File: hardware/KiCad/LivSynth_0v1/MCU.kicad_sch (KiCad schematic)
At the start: 19 parts, among them J2 SWD, J3 USB_B_Micro, SW1 SW_SPDT, U9 STM32F405RGT6, Y1 ABM8-16

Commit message: Fill all title blocks
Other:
- title: (none) -> LivSynth - MCU
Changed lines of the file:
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@@
   (paper "A4")
   (title_block
+    (title "LivSynth - MCU")
     (date "2022-07-18")
     (rev "${Version}")

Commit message: Initial Routing finished
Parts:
- added NT1: NetTie_2, NetTie:NetTie-2_SMD_Pad2.0mm, symbol Device:NetTie_2
- C20: footprint Capacitor_SMD:C_0603_1608Metric_Pad1.08x0.95mm_HandSolder -> Capacitor_THT:CP_Radial_D8.0mm_P5.00mm
- J3: footprint (none) -> Connector_USB:USB_Micro-B_Wuerth_629105150521
- SW1: footprint Capacitor_THT:C_Disc_D3.0mm_W1.6mm_P2.50mm -> Button_Switch_THT:SW_E-Switch_EG1224_SPDT_Angled
- Y1: footprint (none) -> Crystal:Crystal_SMD_3225-4Pin_3.2x2.5mm_HandSoldering
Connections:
- net DAC_OUT2 is gone; now on net SPI_SCK: U9.21 (PA5)
- net CLOCK_OUT: now also U9.24 (PC4); no longer U9.22 (PA6)
- net GATE_OUT: now also U9.26 (PB0); no longer U9.24 (PC4)
- net GND: now also NT1.1; no longer J3.5 (GND)
- net RESET_OUT: now also U9.25 (PC5); no longer U9.23 (PA7)
- net SPI_MISO: now also U9.22 (PA6); no longer U9.52 (PC11)
- net SPI_SCK: no longer U9.51 (PC10)
- net SR_SHLDN: now also U9.11 (PC3); no longer U9.2 (PC13)
- net VCAP_1: now reaches C27.1, U9.31 (VCAP_1)
- net DAC_OUT1: now reaches U9.20 (PA4)
- net VCAP_2: now reaches C28.1, U9.47 (VCAP_2)
- new net: J3.5 (GND), NT1.2
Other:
- moved on the sheet: C18, C19, C20, C21, C22, C23, C24, C25, C26, C27, C28, C29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

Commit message: Rework for polyester film capacitors
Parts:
- C18: footprint Capacitor_THT:C_Disc_D3.0mm_W1.6mm_P2.50mm -> Capacitor_THT:C_Rect_L7.2mm_W2.5mm_P5.00mm_FKS2_FKP2_MKS2_MKP2
- C19: footprint Capacitor_THT:C_Disc_D3.0mm_W1.6mm_P2.50mm -> Capacitor_THT:C_Rect_L7.2mm_W5.5mm_P5.00mm_FKS2_FKP2_MKS2_MKP2
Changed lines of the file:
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@@
       (effects (font (size 1.27 1.27)) (justify left))
     )
-    (property "Footprint" "Capacitor_THT:C_Disc_D3.0mm_W1.6mm_P2.50mm" (id 2) (at 160.02 38.735 0)
+    (property "Footprint" "Capacitor_THT:C_Rect_L7.2mm_W2.5mm_P5.00mm_FKS2_FKP2_MKS2_MKP2" (id 2) (at 160.02 38.735 0)
       (effects (font (size 1.27 1.27)) hide)
     )
@@
       (effects (font (size 1.27 1.27)) (justify left))
     )
-    (property "Footprint" "Capacitor_THT:C_Disc_D3.0mm_W1.6mm_P2.50mm" (id 2) (at 172.085 38.735 0)
-      (effects (font (size 1.27 1.27)) hide)
-    )
+    (property "Footprint" "Capacitor_THT:C_Rect_L7.2mm_W5.5mm_P5.00mm_FKS2_FKP2_MKS2_MKP2" (id 2) (at 172.085 38.735 0)
+      (effects (font (size 1.27 1.27)) hide)
+    )

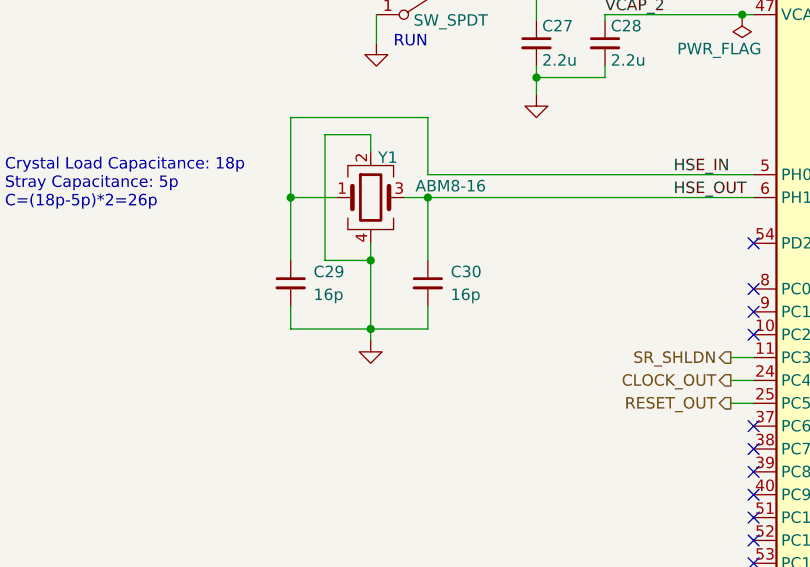
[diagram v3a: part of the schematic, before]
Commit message: Adjust crystal cap values Add BOM csv
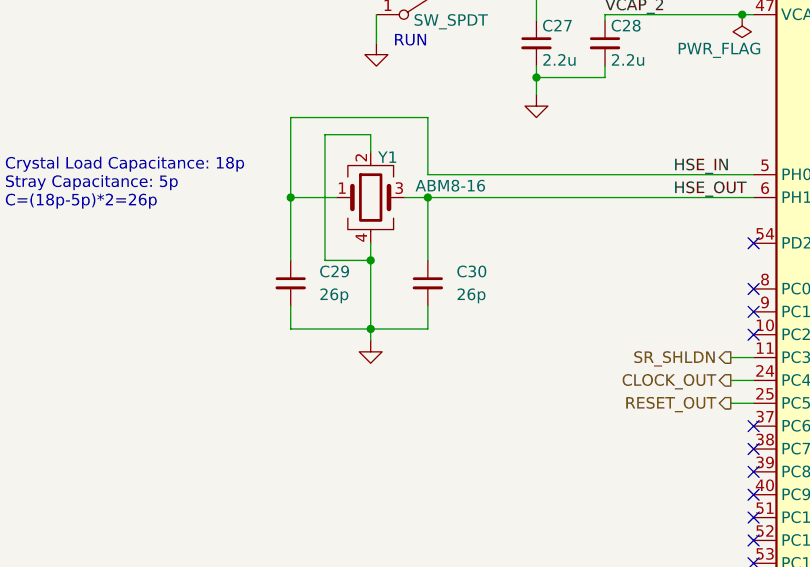
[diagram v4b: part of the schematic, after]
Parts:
- C29, C30: value 16p -> 26p
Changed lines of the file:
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@@
   (symbol (lib_id "Device:C_Small") (at 85.725 93.345 0) (unit 1)
     (in_bom yes) (on_board yes) (fields_autoplaced)
-    (property "Reference" "C30" (id 0) (at 88.265 92.0812 0)
+    (property "Reference" "C30" (id 0) (at 88.9 92.0812 0)
       (effects (font (size 1.27 1.27)) (justify left))
     )
-    (property "Value" "16p" (id 1) (at 88.265 94.6212 0)
+    (property "Value" "26p" (id 1) (at 88.9 94.6212 0)
       (effects (font (size 1.27 1.27)) (justify left))
     )
@@
   (symbol (lib_id "Device:C_Small") (at 70.485 93.345 0) (unit 1)
     (in_bom yes) (on_board yes) (fields_autoplaced)
-    (property "Reference" "C29" (id 0) (at 73.025 92.0812 0)
+    (property "Reference" "C29" (id 0) (at 73.66 92.0812 0)
       (effects (font (size 1.27 1.27)) (justify left))
     )
-    (property "Value" "16p" (id 1) (at 73.025 94.6212 0)
+    (property "Value" "26p" (id 1) (at 73.66 94.6212 0)
       (effects (font (size 1.27 1.27)) (justify left))
     )

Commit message: Use correct Elko sizes (8mm/3.5mm)
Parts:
- C20: footprint Capacitor_THT:CP_Radial_D8.0mm_P5.00mm -> Capacitor_THT:CP_Radial_D8.0mm_P3.50mm
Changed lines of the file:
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@@
       (effects (font (size 1.27 1.27)) (justify left))
     )
-    (property "Footprint" "Capacitor_THT:CP_Radial_D8.0mm_P5.00mm" (id 2) (at 54.61 39.37 0)
+    (property "Footprint" "Capacitor_THT:CP_Radial_D8.0mm_P3.50mm" (id 2) (at 54.61 39.37 0)
       (effects (font (size 1.27 1.27)) hide)
     )

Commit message: 0v1 Ready for Production
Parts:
- renumbered C27 to C32, C25 to C33, C23 to C36, C18 to C37, C28 to C43, C21 to C44, C26 to C45, C22 to C46, C24 to C47, C30 to C48, C19 to C49, C29 to C50, C20 to C51, J3 to J16, J2 to J19, NT1 to NT5, R5 to R93, SW1 to SW7
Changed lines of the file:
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@@
   (symbol (lib_id "Device:NetTie_2") (at 190.5 146.685 90) (unit 1)
     (in_bom yes) (on_board yes)
-    (property "Reference" "NT1" (id 0) (at 191.135 146.685 90)
+    (property "Reference" "NT5" (id 0) (at 191.135 146.685 90)
       (effects (font (size 1.27 1.27)) (justify right))
     )
@@
   (symbol (lib_id "Device:C_Small") (at 91.44 39.37 0) (unit 1)
     (in_bom yes) (on_board yes) (fields_autoplaced)
-    (property "Reference" "C23" (id 0) (at 94.615 38.1062 0)
+    (property "Reference" "C36" (id 0) (at 94.615 38.1062 0)
       (effects (font (size 1.27 1.27)) (justify left))
     )
@@
   (symbol (lib_id "Device:C_Small") (at 160.02 38.735 0) (unit 1)
     (in_bom yes) (on_board yes) (fields_autoplaced)
-    (property "Reference" "C18" (id 0) (at 162.56 37.4712 0)
+    (property "Reference" "C37" (id 0) (at 162.56 37.4712 0)
       (effects (font (size 1.27 1.27)) (justify left))
     )
@@
   (symbol (lib_id "Device:C_Small") (at 97.79 66.675 0) (unit 1)
     (in_bom yes) (on_board yes)
-    (property "Reference" "C27" (id 0) (at 98.425 64.77 0)
+    (property "Reference" "C32" (id 0) (at 98.425 64.77 0)
       (effects (font (size 1.27 1.27)) (justify left))
     )
@@
   (symbol (lib_id "Device:R") (at 107.315 55.88 90) (unit 1)
     (in_bom yes) (on_board yes)
-    (property "Reference" "R5" (id 0) (at 107.315 53.34 90))
+    (property "Reference" "R93" (id 0) (at 107.315 53.34 90))
     (property "Value" "10K" (id 1) (at 107.315 58.42 90))
     (property "Footprint" "Resistor_THT:R_Axial_DIN0207_L6.3mm_D2.5mm_P7.62mm_Horizontal" (id 2) (at 107.315 57.658 90)
@@
   (symbol (lib_id "Device:C_Small") (at 115.57 39.37 0) (unit 1)
     (in_bom yes) (on_board yes) (fields_autoplaced)
-    (property "Reference" "C25" (id 0) (at 118.745 38.1062 0)
+    (property "Reference" "C33" (id 0) (at 118.745 38.1062 0)
       (effects (font (size 1.27 1.27)) (justify left))
     )
@@
   (symbol (lib_id "Connector:Conn_01x06_Male") (at 187.325 88.9 0) (mirror y) (unit 1)
     (in_bom yes) (on_board yes) (fields_autoplaced)
-    (property "Reference" "J2" (id 0) (at 188.595 88.8999 0)
+    (property "Reference" "J19" (id 0) (at 188.595 88.8999 0)
       (effects (font (size 1.27 1.27)) (justify right))
     )
@@
   (symbol (lib_id "Connector:USB_B_Micro") (at 190.5 132.08 0) (mirror y) (unit 1)
     (in_bom yes) (on_board yes) (fields_autoplaced)
-    (property "Reference" "J3" (id 0) (at 197.485 130.8099 0)
+    (property "Reference" "J16" (id 0) (at 197.485 130.8099 0)
       (effects (font (size 1.27 1.27)) (justify right))
     )
@@
   (symbol (lib_id "Device:C_Small") (at 79.375 39.37 0) (unit 1)
     (in_bom yes) (on_board yes) (fields_autoplaced)
-    (property "Reference" "C22" (id 0) (at 82.55 38.1062 0)
+    (property "Reference" "C46" (id 0) (at 82.55 38.1062 0)
       (effects (font (size 1.27 1.27)) (justify left))
     )
@@
   (symbol (lib_id "Device:C_Small") (at 85.725 93.345 0) (unit 1)
     (in_bom yes) (on_board yes) (fields_autoplaced)
-    (property "Reference" "C30" (id 0) (at 88.9 92.0812 0)
+    (property "Reference" "C48" (id 0) (at 88.9 92.0812 0)
       (effects (font (size 1.27 1.27)) (justify left))
     )
@@
   (symbol (lib_id "Device:C_Small") (at 172.085 38.735 0) (unit 1)
     (in_bom yes) (on_board yes) (fields_autoplaced)
-    (property "Reference" "C19" (id 0) (at 175.26 37.4712 0)
+    (property "Reference" "C49" (id 0) (at 175.26 37.4712 0)
       (effects (font (size 1.27 1.27)) (justify left))
     )
@@
   (symbol (lib_id "Device:C_Small") (at 66.675 39.37 0) (unit 1)
     (in_bom yes) (on_board yes) (fields_autoplaced)
-    (property "Reference" "C21" (id 0) (at 69.85 38.1062 0)
+    (property "Reference" "C44" (id 0) (at 69.85 38.1062 0)
       (effects (font (size 1.27 1.27)) (justify left))
     )
@@
   (symbol (lib_id "Switch:SW_SPDT") (at 85.09 60.96 180) (unit 1)
     (in_bom yes) (on_board yes)
-    (property "Reference" "SW1" (id 0) (at 87.63 59.055 0))
+    (property "Reference" "SW7" (id 0) (at 87.63 59.055 0))
     (property "Value" "SW_SPDT" (id 1) (at 88.265 64.135 0))
     (property "Footprint" "Button_Switch_THT:SW_E-Switch_EG1224_SPDT_Angled" (id 2) (at 85.09 60.96 0)
@@
   (symbol (lib_id "Device:C_Small") (at 103.505 39.37 0) (unit 1)
     (in_bom yes) (on_board yes) (fields_autoplaced)
-    (property "Reference" "C24" (id 0) (at 106.68 38.1062 0)
+    (property "Reference" "C47" (id 0) (at 106.68 38.1062 0)
       (effects (font (size 1.27 1.27)) (justify left))
     )
@@
   (symbol (lib_id "Device:C_Small") (at 66.675 54.61 0) (unit 1)
     (in_bom yes) (on_board yes) (fields_autoplaced)
-    (property "Reference" "C26" (id 0) (at 69.85 53.3462 0)
+    (property "Reference" "C45" (id 0) (at 69.85 53.3462 0)
       (effects (font (size 1.27 1.27)) (justify left))
     )
@@
   (symbol (lib_id "Device:C_Small") (at 70.485 93.345 0) (unit 1)
     (in_bom yes) (on_board yes) (fields_autoplaced)
-    (property "Reference" "C29" (id 0) (at 73.66 92.0812 0)
+    (property "Reference" "C50" (id 0) (at 73.66 92.0812 0)
       (effects (font (size 1.27 1.27)) (justify left))
     )
@@
   (symbol (lib_id "Device:C_Polarized_Small") (at 54.61 39.37 0) (unit 1)
     (in_bom yes) (on_board yes) (fields_autoplaced)
-    (property "Reference" "C20" (id 0) (at 57.785 37.5538 0)
+    (property "Reference" "C51" (id 0) (at 57.785 37.5538 0)
       (effects (font (size 1.27 1.27)) (justify left))
     )
@@
   (symbol (lib_id "Device:C_Small") (at 105.41 66.675 0) (unit 1)
     (in_bom yes) (on_board yes)
-    (property "Reference" "C28" (id 0) (at 106.045 64.77 0)
-      (effects (font (size 1.27 1.27)) (justify left))
-    )
+    (property "Reference" "C43" (id 0) (at 106.045 64.77 0)
+      (effects (font (size 1.27 1.27)) (justify left))
+    )
